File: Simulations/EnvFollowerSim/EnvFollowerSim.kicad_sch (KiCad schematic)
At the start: 21 parts, among them U1 TL074

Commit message: compressor sim upgrades
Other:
- moved on the sheet: U1E, V1, V2
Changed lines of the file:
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@@
 	(wire
 		(pts
-			(xy 23.876 115.57) (xy 23.876 117.602)
+			(xy 24.13 85.598) (xy 24.13 87.63)
 		)
 		(stroke
@@
 	(wire
 		(pts
-			(xy 23.876 94.742) (xy 23.876 96.012)
+			(xy 85.09 168.91) (xy 85.09 170.18)
 		)
 		(stroke
@@
 	(wire
 		(pts
-			(xy 33.02 94.996) (xy 33.02 96.266)
+			(xy 94.234 169.164) (xy 94.234 170.434)
 		)
 		(stroke
@@
 	(wire
 		(pts
-			(xy 23.876 132.842) (xy 23.876 134.366)
+			(xy 24.13 102.87) (xy 24.13 104.394)
 		)
 		(stroke
@@
 	(wire
 		(pts
-			(xy 23.876 106.172) (xy 23.876 107.188)
+			(xy 85.09 180.34) (xy 85.09 181.356)
 		)
 		(stroke
@@
 	(wire
 		(pts
-			(xy 33.02 106.426) (xy 33.02 107.442)
+			(xy 94.234 180.594) (xy 94.234 181.61)
 		)
 		(stroke
@@
 	)
 	(label "VG"
-		(at 33.02 94.996 0)
+		(at 94.234 169.164 0)
 		(effects
 			(font
@@
 	(symbol
 		(lib_id "power:+18V")
-		(at 23.876 94.742 0)
+		(at 85.09 168.91 0)
 		(unit 1)
 		(body_style 1)
@@
 		(fields_autoplaced yes)
 		(property "Reference" "#PWR01"
-			(at 23.876 98.552 0)
+			(at 85.09 172.72 0)
 			(hide yes)
 			(show_name no)
@@
 		)
 		(property "Value" "+18V"
-			(at 23.876 90.17 0)
+			(at 85.09 164.338 0)
 			(show_name no)
 			(do_not_autoplace no)
@@
 		)
 		(property "Footprint" ""
-			(at 23.876 94.742 0)
+			(at 85.09 168.91 0)
 			(hide yes)
 			(show_name no)
@@
 		)
 		(property "Datasheet" ""
-			(at 23.876 94.742 0)
+			(at 85.09 168.91 0)
 			(hide yes)
 			(show_name no)
@@
 		)
 		(property "Description" "Power symbol creates a global label with name \"+12V\""
-			(at 23.876 94.742 0)
+			(at 85.09 168.91 0)
 			(hide yes)
 			(show_name no)
@@
 	(symbol
 		(lib_id "power:GND")
-		(at 33.02 107.442 0)
+		(at 94.234 181.61 0)
 		(unit 1)
 		(body_style 1)
@@
 		(fields_autoplaced yes)
 		(property "Reference" "#PWR05"
-			(at 33.02 113.792 0)
+			(at 94.234 187.96 0)
 			(hide yes)
 			(show_name no)
@@
 		)
 		(property "Value" "GND"
-			(at 33.02 111.252 0)
+			(at 94.234 185.42 0)
 			(hide yes)
 			(show_name no)
@@
 		)
 		(property "Footprint" ""
-			(at 33.02 107.442 0)
+			(at 94.234 181.61 0)
 			(hide yes)
 			(show_name no)
@@
 		)
 		(property "Datasheet" ""
-			(at 33.02 107.442 0)
+			(at 94.234 181.61 0)
 			(hide yes)
 			(show_name no)
@@
 		)
 		(property "Description" "Power symbol creates a global label with name \"GND\" , ground"
-			(at 33.02 107.442 0)
+			(at 94.234 181.61 0)
 			(hide yes)
 			(show_name no)
@@
 	(symbol
 		(lib_id "Simulation_SPICE:VDC")
-		(at 33.02 101.346 0)
+		(at 94.234 175.514 0)
 		(unit 1)
 		(body_style 1)
@@
 		(fields_autoplaced yes)
 		(property "Reference" "V2"
-			(at 36.83 99.9461 0)
+			(at 98.044 174.1141 0)
 			(show_name no)
 			(do_not_autoplace no)
@@
 		)
 		(property "Value" "9"
-			(at 36.83 102.4861 0)
+			(at 98.044 176.6541 0)
 			(show_name no)
 			(do_not_autoplace no)
@@
 		)
 		(property "Footprint" ""
-			(at 33.02 101.346 0)
+			(at 94.234 175.514 0)
 			(hide yes)
 			(show_name no)
@@
 		)
 		(property "Datasheet" "https://ngspice.sourceforge.io/docs/ngspice-html-manual/manual.xhtml#sec_Independent_Sources_for"
-			(at 33.02 101.346 0)
+			(at 94.234 175.514 0)
 			(hide yes)
 			(show_name no)
@@
 		)
 		(property "Description" "Voltage source, DC"
-			(at 33.02 101.346 0)
+			(at 94.234 175.514 0)
 			(hide yes)
 			(show_name no)
@@
 		)
 		(property "Sim.Pins" "1=+ 2=-"
-			(at 33.02 101.346 0)
+			(at 94.234 175.514 0)
 			(hide yes)
 			(show_name no)
@@
 		)
 		(property "Sim.Type" "DC"
-			(at 33.02 101.346 0)
+			(at 94.234 175.514 0)
 			(hide yes)
 			(show_name no)
@@
 		)
 		(property "Sim.Device" "V"
-			(at 33.02 101.346 0)
+			(at 94.234 175.514 0)
 			(hide yes)
 			(show_name no)
@@
 	(symbol
 		(lib_id "Amplifier_Operational:TL074")
-		(at 26.416 125.222 0)
+		(at 26.67 95.25 0)
 		(unit 5)
 		(body_style 1)
@@
 		(fields_autoplaced yes)
 		(property "Reference" "U1"
-			(at 24.892 123.9519 0)
+			(at 25.146 93.9799 0)
 			(show_name no)
 			(do_not_autoplace no)
@@
 		)
 		(property "Value" "TL074"
-			(at 24.892 126.4919 0)
+			(at 25.146 96.5199 0)
 			(show_name no)
 			(do_not_autoplace no)
@@
 		)
 		(property "Footprint" ""
-			(at 25.146 122.682 0)
+			(at 25.4 92.71 0)
 			(hide yes)
 			(show_name no)
@@
 		)
 		(property "Datasheet" "http://www.ti.com/lit/ds/symlink/tl071.pdf"
-			(at 27.686 120.142 0)
+			(at 27.94 90.17 0)
 			(hide yes)
 			(show_name no)
@@
 		)
 		(property "Description" "Quad Low-Noise JFET-Input Operational Amplifiers, DIP-14/SOIC-14"
-			(at 26.416 125.222 0)
+			(at 26.67 95.25 0)
 			(hide yes)
 			(show_name no)
@@
 		)
 		(property "Sim.Library" "/Users/hayden/dev/STM32_Projects/CompressorPedal/CompressorSim/tl074-quad.lib"
-			(at 26.416 125.222 0)
+			(at 26.67 95.25 0)
 			(hide yes)
 			(show_name no)
@@
 		)
 		(property "Sim.Name" "TL074c"
-			(at 26.416 125.222 0)
+			(at 26.67 95.25 0)
 			(hide yes)
 			(show_name no)
@@
 		)
 		(property "Sim.Device" "SUBCKT"
-			(at 26.416 125.222 0)
+			(at 26.67 95.25 0)
 			(hide yes)
 			(show_name no)
@@
 		)
 		(property "Sim.Pins" "1=1 2=2 3=3 4=4 5=5 6=6 7=7 8=8 9=9 10=10 11=11 12=12 13=13 14=14"
-			(at 26.416 125.222 0)
+			(at 26.67 95.25 0)
 			(hide yes)
 			(show_name no)
@@
 	(symbol
 		(lib_id "power:GND")
-		(at 23.876 134.366 0)
+		(at 24.13 104.394 0)
 		(unit 1)
 		(body_style 1)
@@
 		(fields_autoplaced yes)
 		(property "Reference" "#PWR04"
-			(at 23.876 140.716 0)
+			(at 24.13 110.744 0)
 			(hide yes)
 			(show_name no)
@@
 		)
 		(property "Value" "GND"
-			(at 23.876 138.176 0)
+			(at 24.13 108.204 0)
 			(hide yes)
 			(show_name no)
@@
 		)
 		(property "Footprint" ""
-			(at 23.876 134.366 0)
+			(at 24.13 104.394 0)
 			(hide yes)
 			(show_name no)
@@
 		)
 		(property "Datasheet" ""
-			(at 23.876 134.366 0)
+			(at 24.13 104.394 0)
 			(hide yes)
 			(show_name no)
@@
 		)
 		(property "Description" "Power symbol creates a global label with name \"GND\" , ground"
-			(at 23.876 134.366 0)
+			(at 24.13 104.394 0)
 			(hide yes)
 			(show_name no)
@@
 	(symbol
 		(lib_id "Simulation_SPICE:VDC")
-		(at 23.876 101.092 0)
+		(at 85.09 175.26 0)
 		(unit 1)
 		(body_style 1)
@@
 		(fields_autoplaced yes)
 		(property "Reference" "V1"
-			(at 27.94 99.6921 0)
+			(at 89.154 173.8601 0)
 			(show_name no)
 			(do_not_autoplace no)
@@
 		)
 		(property "Value" "18"
-			(at 27.94 102.2321 0)
+			(at 89.154 176.4001 0)
 			(show_name no)
 			(do_not_autoplace no)
@@
 		)
 		(property "Footprint" ""
-			(at 23.876 101.092 0)
+			(at 85.09 175.26 0)
 			(hide yes)
 			(show_name no)
@@
 		)
 		(property "Datasheet" "https://ngspice.sourceforge.io/docs/ngspice-html-manual/manual.xhtml#sec_Independent_Sources_for"
-			(at 23.876 101.092 0)
+			(at 85.09 175.26 0)
 			(hide yes)
 			(show_name no)
@@
 		)
 		(property "Description" "Voltage source, DC"
-			(at 23.876 101.092 0)
+			(at 85.09 175.26 0)
 			(hide yes)
 			(show_name no)
@@
 		)
 		(property "Sim.Pins" "1=+ 2=-"
-			(at 23.876 101.092 0)
+			(at 85.09 175.26 0)
 			(hide yes)
 			(show_name no)
@@
 		)
 		(property "Sim.Type" "DC"
-			(at 23.876 101.092 0)
+			(at 85.09 175.26 0)
 			(hide yes)
 			(show_name no)
@@
 		)
 		(property "Sim.Device" "V"
-			(at 23.876 101.092 0)
+			(at 85.09 175.26 0)
 			(hide yes)
 			(show_name no)
@@
 	(symbol
 		(lib_id "power:GND")
-		(at 23.876 107.188 0)
+		(at 85.09 181.356 0)
 		(unit 1)
 		(body_style 1)
@@
 		(fields_autoplaced yes)
 		(property "Reference" "#PWR02"
-			(at 23.876 113.538 0)
+			(at 85.09 187.706 0)
 			(hide yes)
 			(show_name no)
@@
 		)
 		(property "Value" "GND"
-			(at 23.876 110.998 0)
+			(at 85.09 185.166 0)
 			(hide yes)
 			(show_name no)
@@
 		)
 		(property "Footprint" ""
-			(at 23.876 107.188 0)
+			(at 85.09 181.356 0)
 			(hide yes)
 			(show_name no)
@@
 		)
 		(property "Datasheet" ""
-			(at 23.876 107.188 0)
+			(at 85.09 181.356 0)
 			(hide yes)
 			(show_name no)
@@
 		)
 		(property "Description" "Power symbol creates a global label with name \"GND\" , ground"
-			(at 23.876 107.188 0)
+			(at 85.09 181.356 0)
 			(hide yes)
 			(show_name no)
@@
 	(symbol
 		(lib_id "power:+18V")
-		(at 23.876 115.57 0)
+		(at 24.13 85.598 0)
 		(unit 1)
 		(body_style 1)
@@
 		(fields_autoplaced yes)
 		(property "Reference" "#PWR03"
-			(at 23.876 119.38 0)
+			(at 24.13 89.408 0)
 			(hide yes)
 			(show_name no)
@@
 		)
 		(property "Value" "+18V"
-			(at 23.876 110.998 0)
+			(at 24.13 81.026 0)
 			(show_name no)
 			(do_not_autoplace no)
@@
 		)
 		(property "Footprint" ""
-			(at 23.876 115.57 0)
+			(at 24.13 85.598 0)
 			(hide yes)
 			(show_name no)
@@
 		)
 		(property "Datasheet" ""
-			(at 23.876 115.57 0)
+			(at 24.13 85.598 0)
 			(hide yes)
 			(show_name no)
@@
 		)
 		(property "Description" "Power symbol creates a global label with name \"+12V\""
-			(at 23.876 115.57 0)
+			(at 24.13 85.598 0)
 			(hide yes)
 			(show_name no)

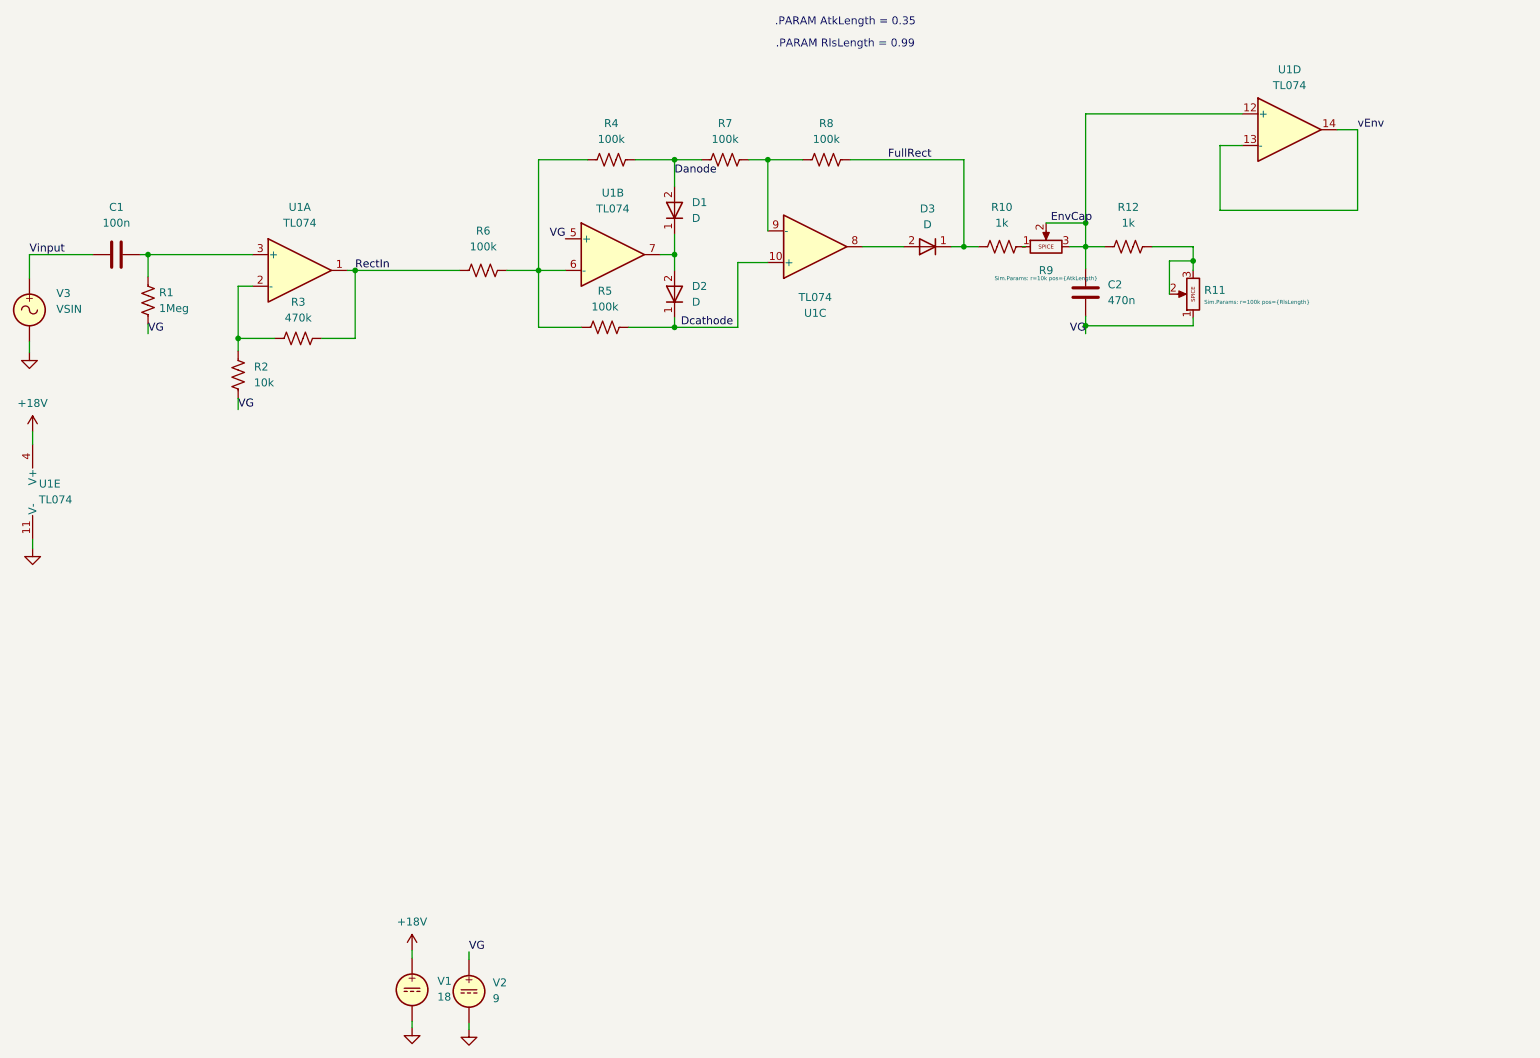
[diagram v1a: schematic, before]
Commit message: updated env. follower and ADC driver in schem
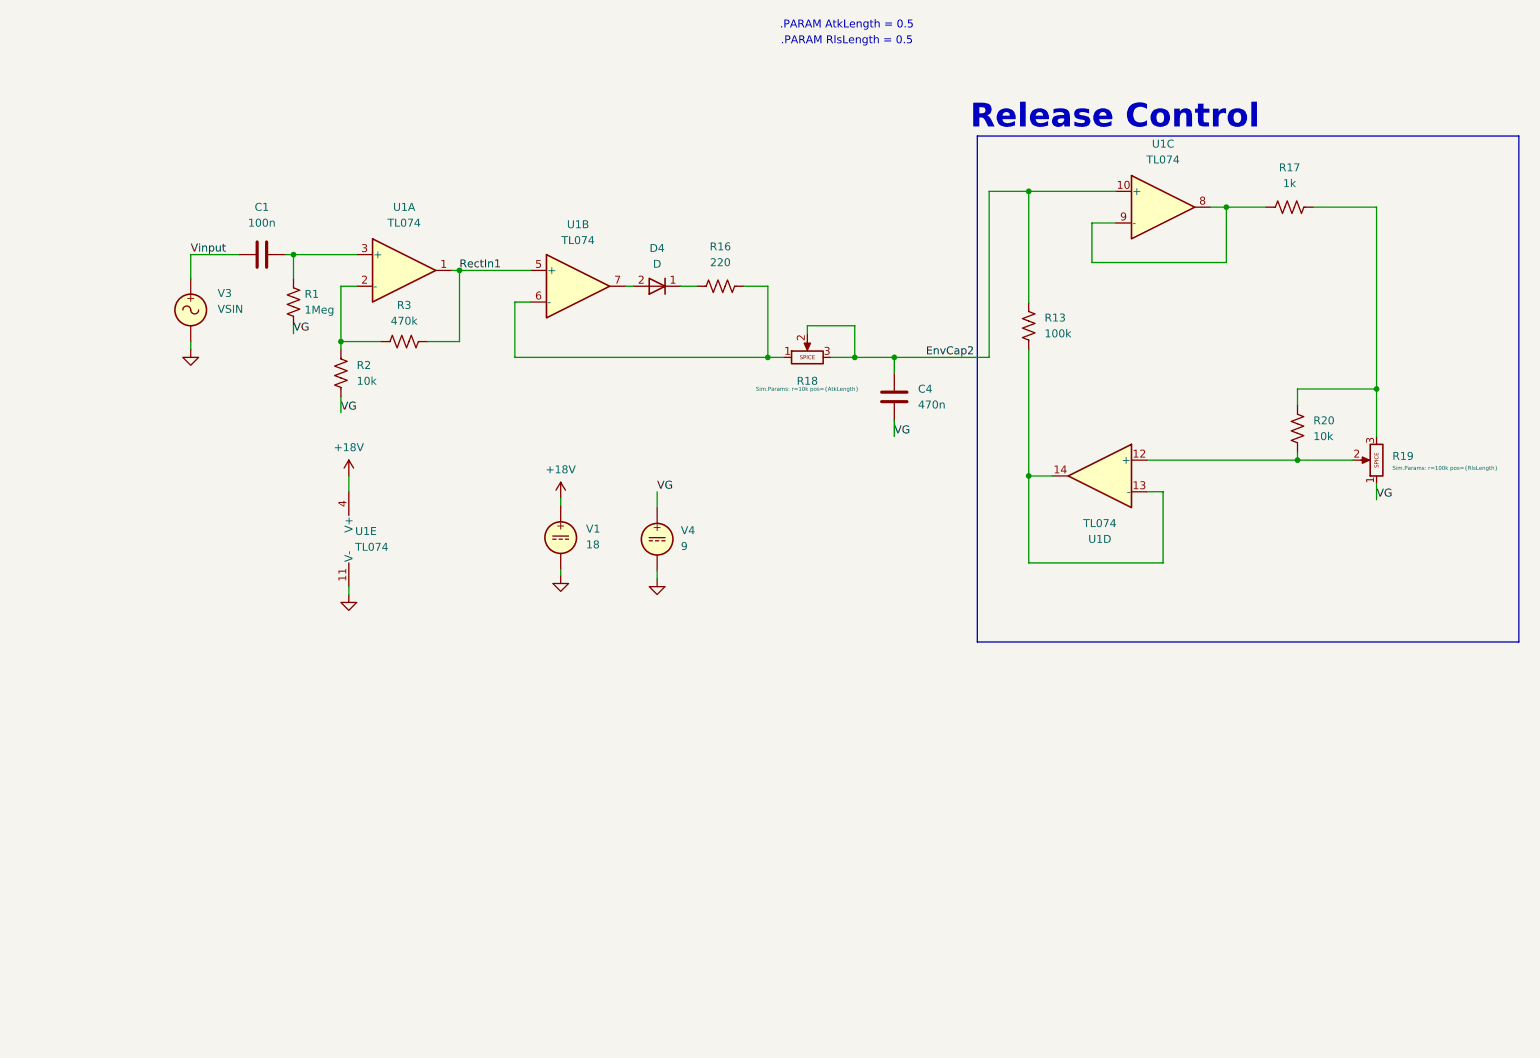
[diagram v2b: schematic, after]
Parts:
- removed C2: 470n, symbol Device:C
- removed D1, D2, D3: D, symbol Simulation_SPICE:D
- removed R10, R12: 1k, symbol Device:R_US
- removed R11, R9: Potentiometer, symbol Simulation_SPICE:Potentiometer
- removed R4, R5, R6, R7, R8: 100k, symbol Device:R_US
- removed V2: 9, symbol Simulation_SPICE:VDC
- added C4: 470n, symbol Device:C
- added D4: D, symbol Simulation_SPICE:D
- added R13: 100k, symbol Device:R_US
- added R16: 220, symbol Device:R_US
- added R17: 1k, symbol Device:R_US
- added R18, R19: Potentiometer, symbol Simulation_SPICE:Potentiometer
- added R20: 10k, symbol Device:R_US
- added V4: 9, symbol Simulation_SPICE:VDC
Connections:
- net GND: now also V4.2
- net VG: now also C4.2, R19.1, V4.1; no longer U1.5 (+)
- net at U1.8: now also U1.9 (-), R17.1
- net at U1.7: now also D4.2 (A)
- net at U1.6 (-): now also R16.2, R18.1
- net Dcathode renamed EnvCap2
- net EnvCap2: now also C4.1, R13.1, R18.2, R18.3
- net EnvCap: no longer names the net of U1.12 (+)
- net EnvCap: now also R19.2, R20.1
- net RectIn renamed RectIn1
- net RectIn1: now also U1.5 (+)
- net vEnv: no longer names the net of U1.13 (-), U1.14
- net vEnv: now also R13.2
- new net: R17.2, R19.3, R20.2
- new net: D4.1 (K), R16.1
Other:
- note added: ".PARAM AtkLength = 0.5"
- note added: ".PARAM RlsLength = 0.5"
- note added: "Release Control"
- note removed: ".PARAM AtkLength = 0.35"
- note removed: ".PARAM RlsLength = 0.99"
- moved on the sheet: C1, R1, R2, R3, U1A, U1B, U1E, V1, V3
